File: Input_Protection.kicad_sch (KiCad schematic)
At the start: 5 parts, among them Q11 STD35P6LLF6

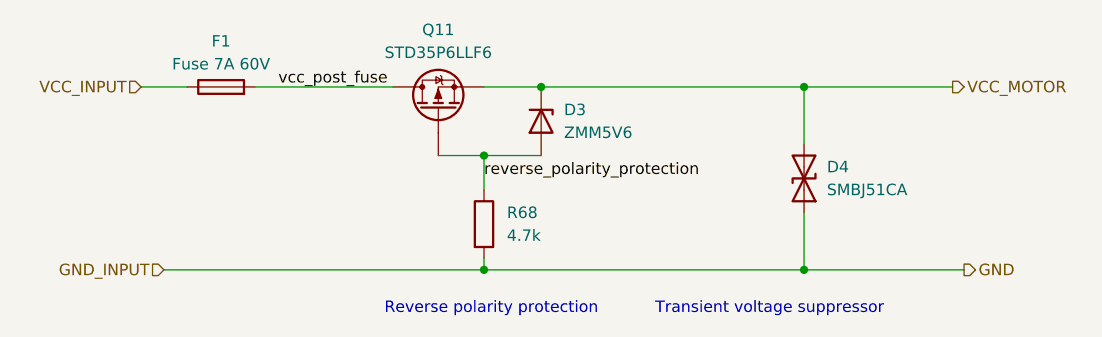
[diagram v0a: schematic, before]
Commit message: Refactored top sheet
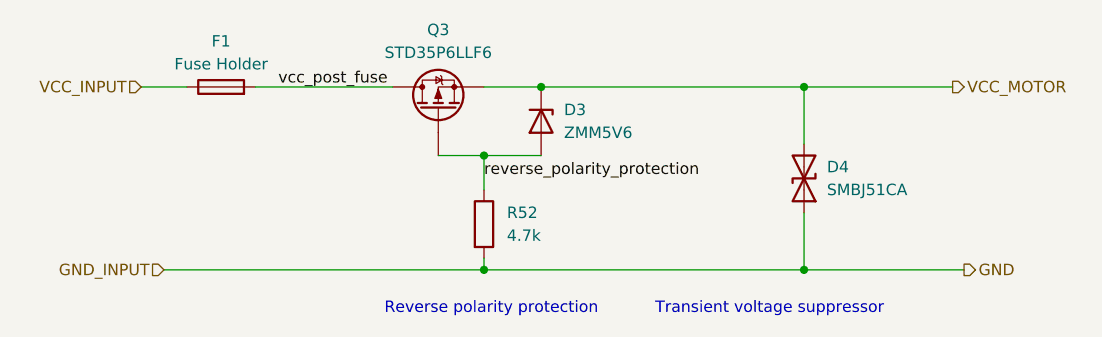
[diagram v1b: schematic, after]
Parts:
- F1: value Fuse 7A 60V -> Fuse Holder
- renumbered Q11 to Q3, R68 to R52
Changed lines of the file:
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@@
   (symbol (lib_id "PersonnalSymbolLibrary:STD35P6LLF6") (at 133.35 58.42 90) (unit 1)
     (in_bom yes) (on_board yes)
-    (property "Reference" "Q11" (id 0) (at 133.35 49.53 90))
+    (property "Reference" "Q3" (id 0) (at 133.35 49.53 90))
     (property "Value" "STD35P6LLF6" (id 1) (at 133.35 52.07 90))
     (property "Footprint" "Package_TO_SOT_SMD:TO-252-2" (id 2) (at 151.13 58.42 0)
@@
   (symbol (lib_id "Device:R") (at 138.43 71.12 0) (unit 1)
     (in_bom yes) (on_board yes) (fields_autoplaced)
-    (property "Reference" "R68" (id 0) (at 140.97 69.8499 0)
+    (property "Reference" "R52" (id 0) (at 140.97 69.8499 0)
       (effects (font (size 1.27 1.27)) (justify left))
     )
@@
     (in_bom yes) (on_board yes)
     (property "Reference" "F1" (id 0) (at 109.22 50.8 90))
-    (property "Value" "Fuse 7A 60V" (id 1) (at 109.22 53.34 90))
+    (property "Value" "Fuse Holder" (id 1) (at 109.22 53.34 90))
     (property "Footprint" "PersonnalFootprintLibrary:Fuse_Littelfuse_178.6764.0001" (id 2) (at 109.22 57.658 90)
       (effects (font (size 1.27 1.27)) hide)
